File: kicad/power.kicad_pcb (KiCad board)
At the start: 2 copper layers, 84.1 x 61.7 mm, 50 parts, among them J1 Bus_PCI_Express_x1, J2 wago 2060-452/998-404, J3 wago 2060-452/998-404, J4 Conn_01x04, J5 Conn_01x02_Pin, J6 USB_C_Receptacle_USB2.0_16P, Q1 SI7232DN-T1-GE3, U2 RP2040, U4 W25Q128JVP, U9 MCP25625T-E/ML, X1 RP2040 Crystal, Y2 X322516MLB4SI

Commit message: add hierarchical sheets
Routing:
- net Net-(J2-1_1): vias 8 -> 4
- net (no net): vias 0 -> 4

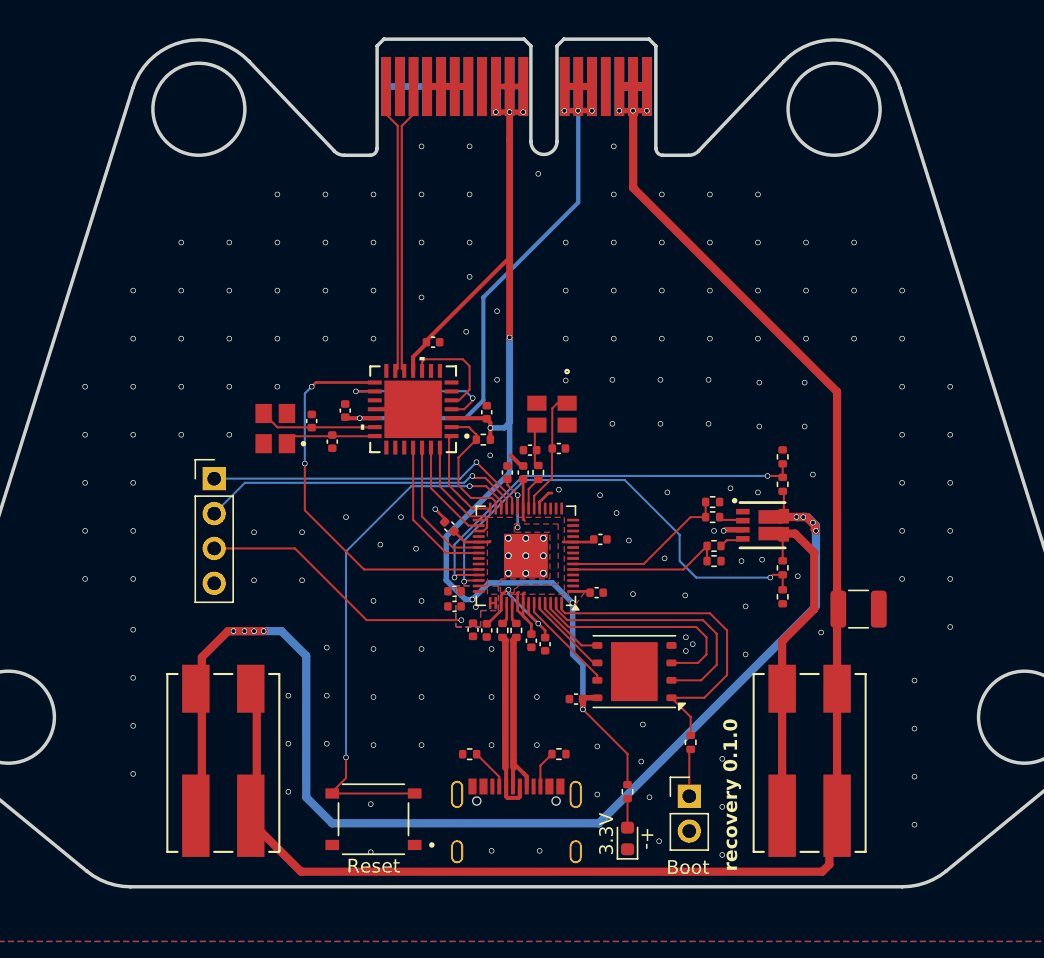
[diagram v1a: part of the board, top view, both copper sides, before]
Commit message: add new ICs to library
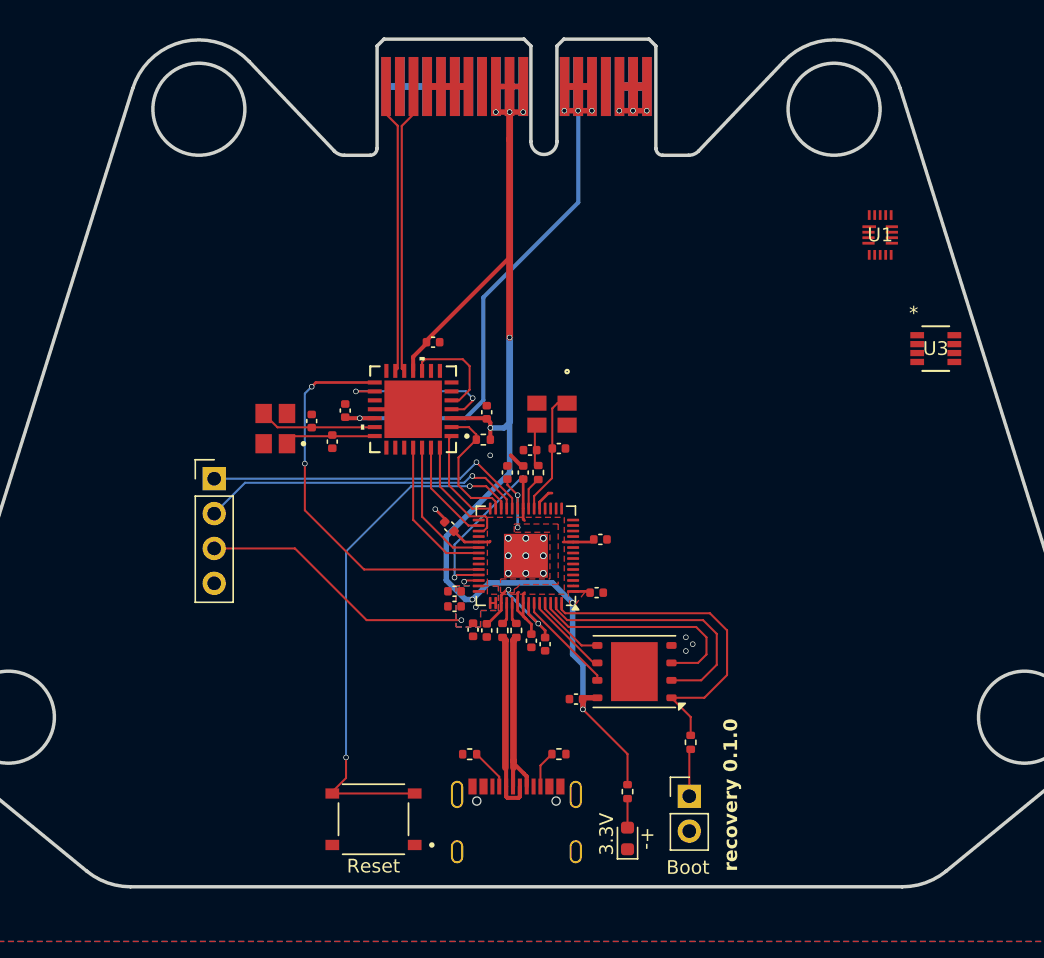
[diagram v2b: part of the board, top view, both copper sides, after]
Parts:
- removed C1: 100u, Capacitor_SMD:C_1210_3225Metric
- removed J2, J3: wago 2060-452/998-404, 4in-recovery:wago-2060-452_998-404
- removed Q1: SI7232DN-T1-GE3, 4in-recovery:SI7232DN-T1-GE3
- removed R20, R300: 100, Resistor_SMD:R_0402_1005Metric
- removed R21, R31: 3.3k, Resistor_SMD:R_0402_1005Metric
- removed R22, R32: 100k, Resistor_SMD:R_0402_1005Metric
- removed R23, R33: 27k, Resistor_SMD:R_0402_1005Metric
- added U1: MP2672GD-0000-Z, 4in-power:QFN-18_2MMx3MM_MP2672_MNP_MPS, F.Cu at (172.9, 75.0)
- added U3: MP2236CGJ-Z, 4in-power:TSOT23-8_MP2236C_MNP, F.Cu at (176.9, 83.2)
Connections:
- net /QSPI_SCLK renamed /digital/QSPI_SCLK
- net /QSPI_SD0 renamed /digital/QSPI_SD0
- net /QSPI_SD1 renamed /digital/QSPI_SD1
- net /QSPI_SD2 renamed /digital/QSPI_SD2
- net /QSPI_SD3 renamed /digital/QSPI_SD3
- net /QSPI_SS renamed /digital/QSPI_SS
- net /RUN renamed /digital/RUN
- net /SWCLK renamed /digital/SWCLK
- net /SWD renamed /digital/SWD
- net /USB_D2+ renamed /digital/USB_D2+
- net /USB_D2- renamed /digital/USB_D2-
- net /XIN renamed /digital/XIN
- net /XOUT renamed /digital/XOUT
- net /XOUT_pre renamed /digital/XOUT_pre
- net /~{USB_BOOT_S} renamed /digital/~{USB_BOOT_S}
- net CANINT renamed /digital/CANINT
- net CANRESET renamed /digital/CANRESET
- net CANSTBY renamed /digital/CANSTBY
- net CS renamed /digital/CS
- net OSC1 renamed /digital/OSC1
- net OSC2 renamed /digital/OSC2
- net SCK renamed /digital/SCK
- net SI renamed /digital/SI
- net SO renamed /digital/SO
- net rx renamed /digital/rx
- net tx renamed /digital/tx
- J1 pad A16: v_lipo -> unconnected-(J1-VBAT-PadA16)
- J1 pad A17: v_lipo -> unconnected-(J1-VBAT-PadA17)
- J1 pad A18: v_lipo -> unconnected-(J1-VBAT-PadA18)
- J1 pad B16: v_lipo -> unconnected-(J1-VBAT-PadB16)
- J1 pad B17: v_lipo -> unconnected-(J1-VBAT-PadB17)
- J1 pad B18: v_lipo -> unconnected-(J1-VBAT-PadB18)
- J6 pad A4: unconnected-(J6-VBUS-PadA4)_3 -> /VBUS
- J6 pad A9: unconnected-(J6-VBUS-PadA4)_2 -> /VBUS
- R204 pad 1: /USB_D- -> /USB_D+
- U2 pad 39: sense_m -> /digital/sense_m
- U2 pad 40: sense_d -> /digital/sense_d
- U2 pad 5: fire_d -> unconnected-(U2-GPIO3-Pad5)
- U2 pad 6: fire_m -> unconnected-(U2-GPIO4-Pad6)
- U9 pad 12: CANL -> /digital/CANL
- U9 pad 13: CANH -> /digital/CANH
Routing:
- net v_lipo: track 119.1 -> 0.00 mm, vias 3 -> 0
- net Net-(J2-1_1): track 92.3 -> 0.00 mm, vias 4 -> 0
- net sense_d: track 34.3 -> 0.00 mm, vias 2 -> 0
- net sense_m: track 31.2 -> 0.00 mm, vias 2 -> 0
- net Net-(J3-1_1): track 25.5 -> 0.00 mm
- net fire_m: track 12.2 -> 0.00 mm
- net fire_d: track 11.6 -> 0.00 mm
- net /digital/sense_m: track 0.00 -> 11.3 mm, vias 0 -> 1
- net (no net): track 0.00 -> 6.00 mm, vias 4 -> 3
- net Net-(Q1-Pad4): track 1.81 -> 0.00 mm
- net Net-(Q1-Pad2): track 1.80 -> 0.00 mm
- net GND: track 17.7 -> 16.3 mm, vias 178 -> 14
- net /digital/sense_d: track 0.00 -> 1.10 mm, vias 0 -> 1

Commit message: update anotations
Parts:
- removed C10, C11: 15p, Capacitor_SMD:C_0402_1005Metric
- removed C206, C207, C209, C211, C212, C213, C214, C215, C216, C40, C90, C92, C93: 100n, Capacitor_SMD:C_0402_1005Metric
- removed C208, C210: 1u, Capacitor_SMD:C_0402_1005Metric
- removed C94, C95: 22p, Capacitor_SMD:C_0402_1005Metric
- removed J4: Conn_01x04, Connector_PinHeader_2.54mm:PinHeader_1x04_P2.54mm_Vertical
- removed J5: Conn_01x02_Pin, Connector_PinHeader_2.54mm:PinHeader_1x02_P2.54mm_Vertical
- removed R12, R30: 1k, Resistor_SMD:R_0402_1005Metric
- removed R203, R204: 27, Resistor_SMD:R_0402_1005Metric
- removed R91: 10k, Resistor_SMD:R_0402_1005Metric
- removed S2: TS-1187A-B-A-B, 4in-kicad-library:TS-1187A-B-A-B
- removed U2: RP2040, Package_DFN_QFN:QFN-56-1EP_7x7mm_P0.4mm_EP3.2x3.2mm
- removed U4: W25Q128JVP, Package_SON:WSON-8-1EP_6x5mm_P1.27mm_EP3.4x4.3mm
- removed U9: MCP25625T-E/ML, 4in-kicad-library:QFN28_6X6MC_MCH
- removed X1: RP2040 Crystal, 4in-kicad-library:ABM8-272-T3_ABR
- removed Y2: X322516MLB4SI, 4in-kicad-library:X322516MLB4SI
- moved U1 32.2 mm to (149.1, 96.7)
- moved D1 28.8 mm to (149.0, 90.7), turned to 0 degrees
- moved U3 26.4 mm to (154.0, 96.3)
- moved R2 25.8 mm to (137.5, 96.1), turned to 0 degrees
- moved R3 19.0 mm to (137.5, 98.1)
- moved R4 13.8 mm to (137.5, 100.1)
- moved J6 3.31 mm to (149.7, 118.0)
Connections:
- J1 pad A1: CANH -> unconnected-(J1-CANH-PadA1)
- J1 pad A3: CANL -> unconnected-(J1-CANN-PadA3)
- U1 pad 1: unconnected-(U1-IN-Pad1) -> /power/VBUS
- U1 pad 10: unconnected-(U1-BATT-Pad10) -> Net-(BT1-+)
- U1 pad 11: unconnected-(U1-SYS-Pad11) -> /power/VSYS
- U1 pad 13: unconnected-(U1-PGND-Pad13) -> GND
- U1 pad 16: unconnected-(U1-*STAT-Pad16) -> Net-(U1-*STAT)
- U1 pad 17: unconnected-(U1-CV-Pad17) -> Net-(U1-CV)
- U1 pad 18: unconnected-(U1-*ACOK-Pad18) -> Net-(U1-*ACOK)
- U1 pad 2: unconnected-(U1-SW-Pad2) -> Net-(C24-Pad1)
- U1 pad 3: unconnected-(U1-BST-Pad3) -> Net-(U1-BST)
- U1 pad 4: unconnected-(U1-VCC-Pad4) -> Net-(U1-VCC)
- U1 pad 5: unconnected-(U1-ISET-Pad5) -> Net-(U1-ISET)
- U1 pad 6: unconnected-(U1-AGND-Pad6) -> AGND
- U1 pad 7: unconnected-(U1-VLIM-Pad7) -> Net-(U1-VLIM)
- U1 pad 8: unconnected-(U1-NTC-Pad8) -> /power/VCC
- U1 pad 9: unconnected-(U1-MID-Pad9) -> Net-(BT1--)
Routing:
- net +3.3V: track 132.6 -> 11.7 mm, vias 10 -> 3
- net /digital/RUN: track 38.3 -> 0.00 mm, vias 2 -> 0
- net +5V: track 43.2 -> 14.2 mm, vias 4 -> 3
- net /digital/CANSTBY: track 28.4 -> 0.00 mm, vias 2 -> 0
- net /digital/QSPI_SS: track 24.5 -> 0.00 mm
- net /digital/SWCLK: track 24.0 -> 0.00 mm, vias 1 -> 0
- net /digital/SWD: track 23.8 -> 0.00 mm, vias 1 -> 0
- net CANH: track 21.1 -> 0.00 mm
- net CANL: track 21.1 -> 0.00 mm
- net /digital/QSPI_SD1: track 18.9 -> 0.00 mm
- net /digital/QSPI_SD2: track 16.7 -> 0.00 mm
- net +1V1: track 14.4 -> 0.00 mm, vias 4 -> 0
- net /USB_D-: track 13.4 -> 0.00 mm
- net /USB_D+: track 13.2 -> 0.00 mm
- net /digital/tx: track 12.1 -> 0.00 mm, vias 2 -> 0
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- removed copper zone on F.Cu, net +1V1
- removed copper zone on B.Cu, net +3.3V
- removed copper zone on F.Cu, net +3.3V
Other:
- board text removed: "+-"
- board text removed: "3.3V"
- board text removed: "recovery 0.1.0"

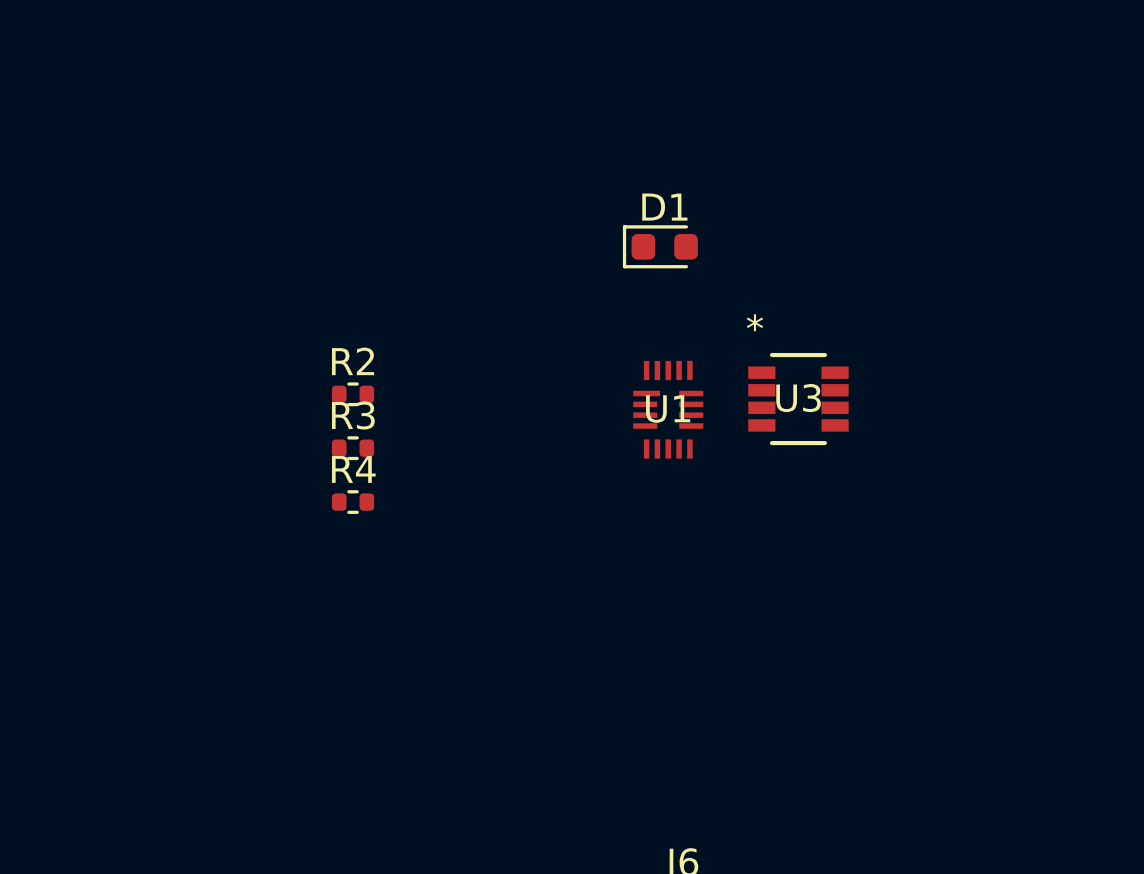
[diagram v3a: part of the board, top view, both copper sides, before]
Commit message: add MB30 connector
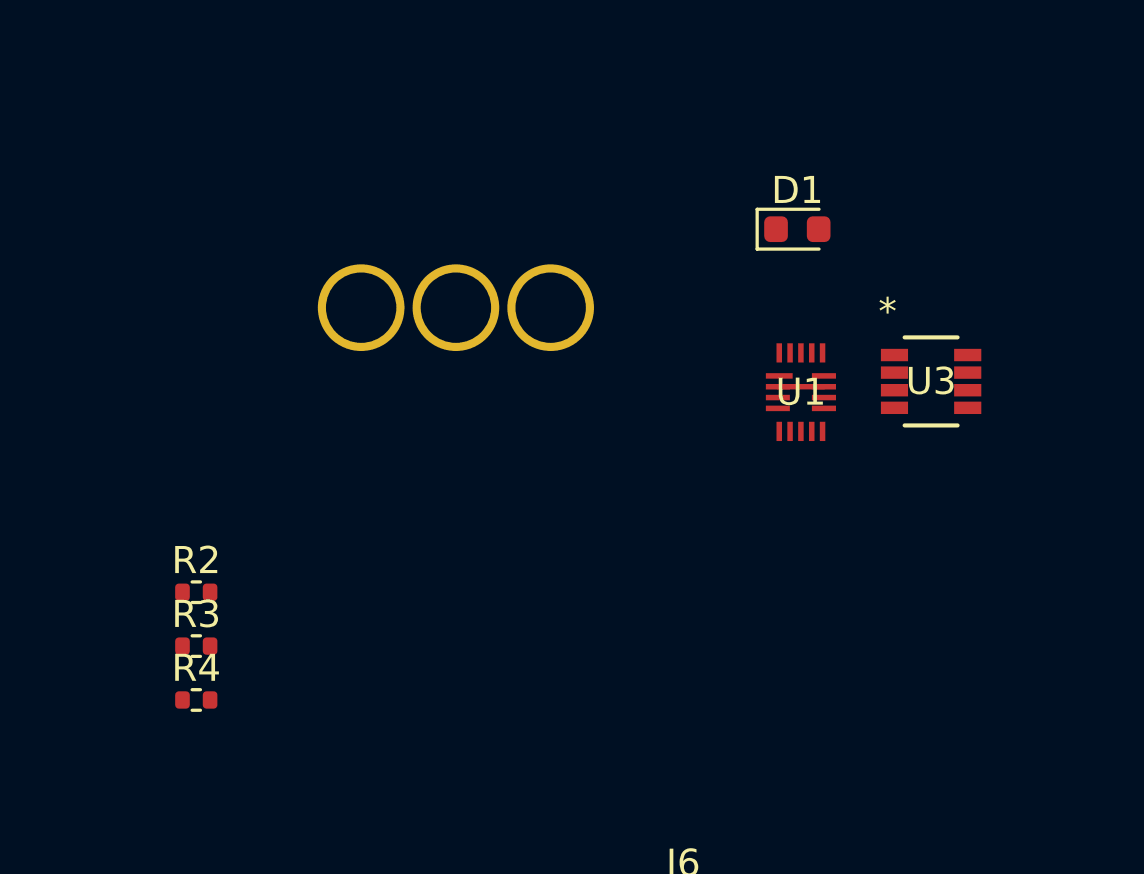
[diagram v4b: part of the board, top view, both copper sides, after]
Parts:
- added U301: MR30-Vertical, 4in-power:CONN-TH_MR30-Vertical, B.Cu at (141.3, 92.9)
- moved R2 9.33 mm to (131.7, 103.4)
- moved R3 9.33 mm to (131.7, 105.4)
- moved R4 9.33 mm to (131.7, 107.4)
- moved D1 4.94 mm to (153.9, 90.0)
- moved U1 4.94 mm to (154.0, 96.0)
- moved U3 4.94 mm to (158.9, 95.6)
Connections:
- J6 pad A6: /USB_D+ -> unconnected-(J6-D+-PadA6)
- J6 pad A7: /USB_D- -> unconnected-(J6-D--PadA7)
- J6 pad B6: /USB_D+ -> unconnected-(J6-D+-PadB6)
- J6 pad B7: /USB_D- -> unconnected-(J6-D--PadB7)
- U1 pad 12: unconnected-(U1-SW-Pad12) -> Net-(C24-Pad1)
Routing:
- net Net-(C24-Pad1): track 0.00 -> 1.70 mm

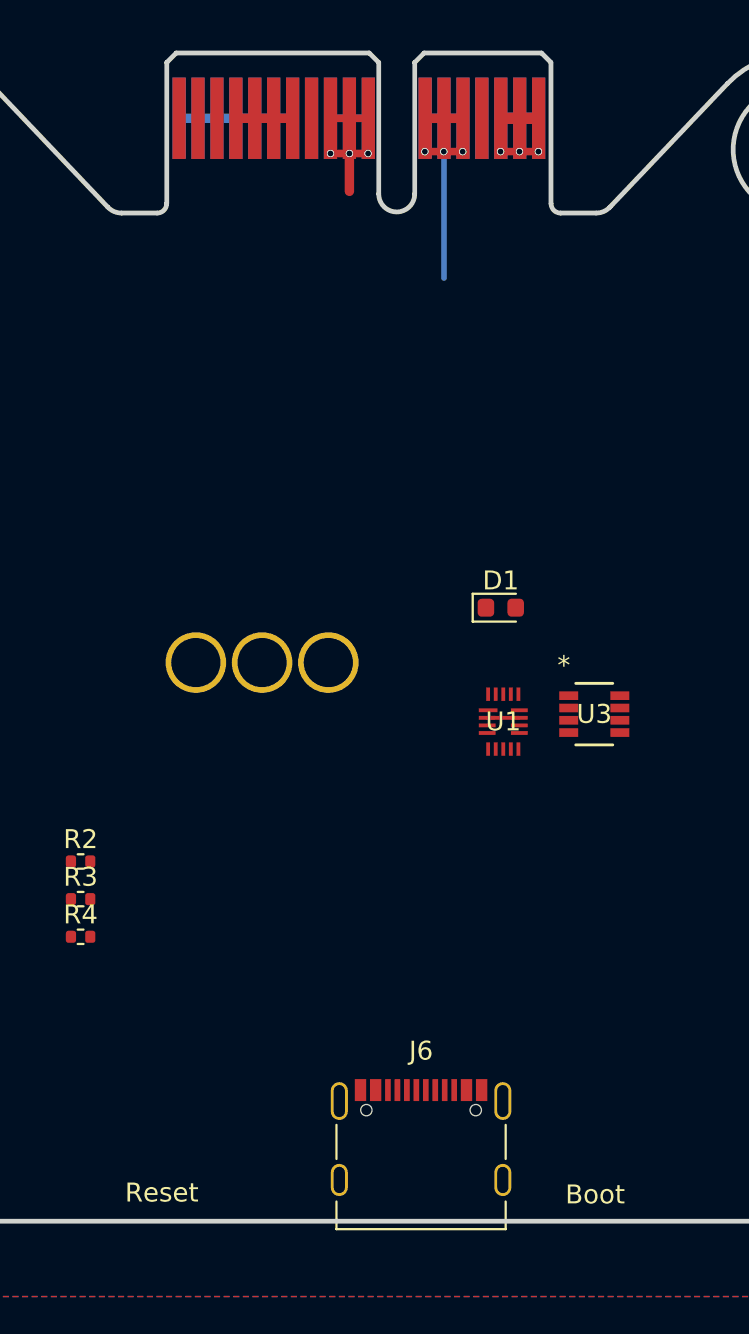
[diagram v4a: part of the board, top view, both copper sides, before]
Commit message: update symbol data fields, add lcsc PN and links
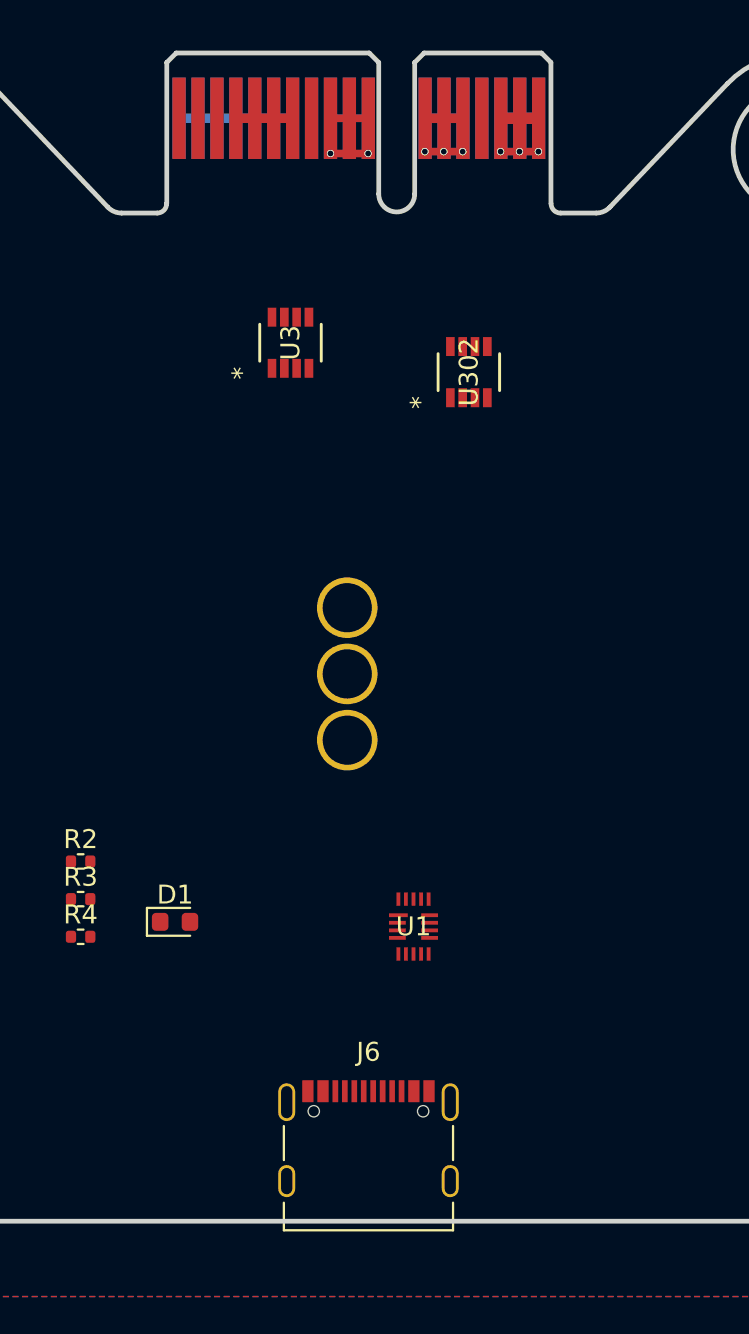
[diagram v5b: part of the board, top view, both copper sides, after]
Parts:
- added U302: MP2236CGJ-Z, 4in-power:TSOT23-8_MP2236C_MNP, F.Cu at (152.2, 77.6)
- moved U3 25.4 mm to (142.8, 76.0), turned to 90 degrees
- moved D1 23.9 mm to (136.7, 106.6)
- moved U1 11.8 mm to (149.3, 106.8)
- moved U301 4.54 mm to (145.8, 93.5), turned to 90 degrees
- moved J6 2.78 mm to (146.9, 118.1)
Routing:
- net +5V: track 14.2 -> 5.71 mm
- net +3.3V: track 11.7 -> 7.85 mm, vias 3 -> 2
- net Net-(C24-Pad1): track 1.70 -> 0.00 mm
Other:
- board text removed: "Boot"
- board text removed: "Reset"
